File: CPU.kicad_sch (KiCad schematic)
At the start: 208 parts, among them P1 Conn_02x36_Top_Bottom, P10 Conn_02x08_Counter_Clockwise, P2 Conn_02x13_Top_Bottom, P3 Conn_02x13_Top_Bottom, P4 Conn_02x08_Counter_Clockwise, P5 Conn_02x25_Counter_Clockwise, P6 Conn_02x25_Counter_Clockwise, P7 Conn_02x07_Counter_Clockwise, P8 Conn_02x08_Counter_Clockwise

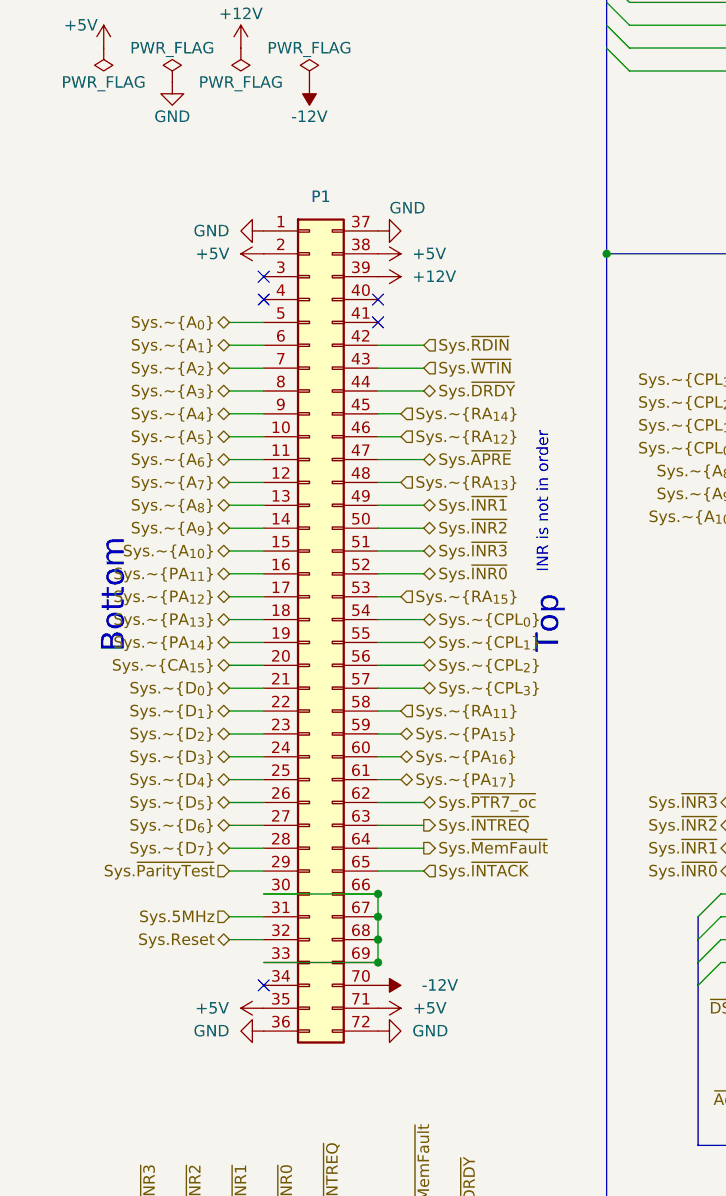
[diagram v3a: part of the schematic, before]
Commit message: Replace edge connector with pin headers
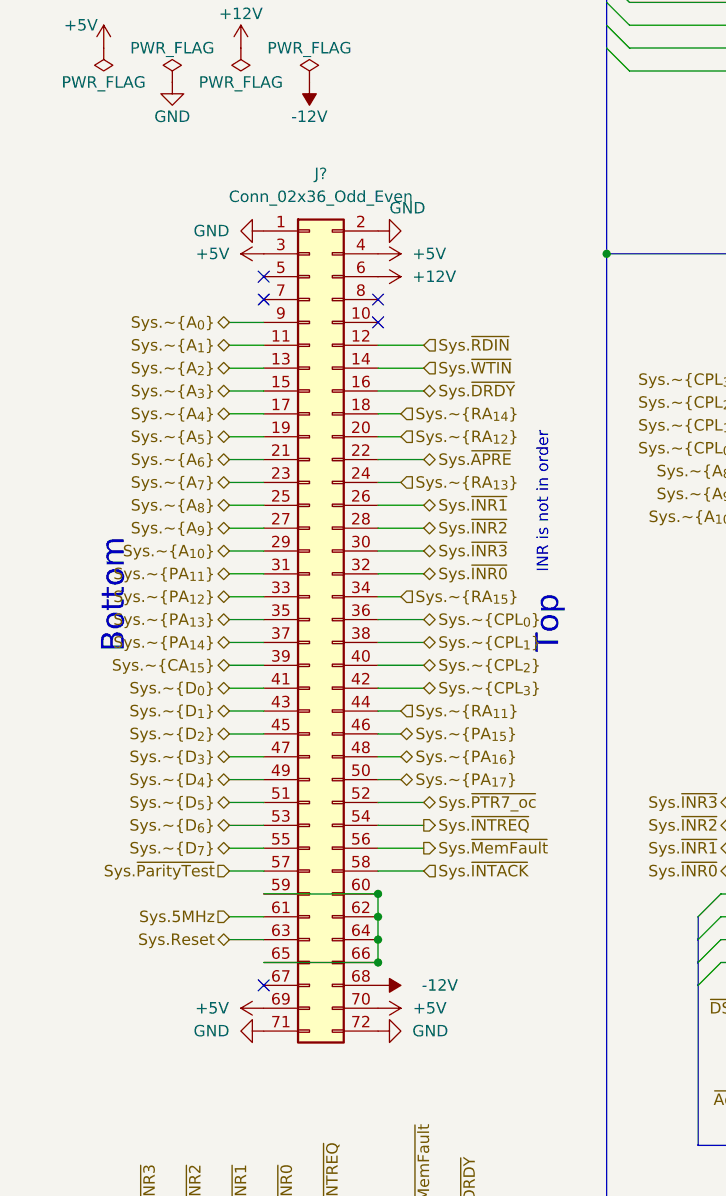
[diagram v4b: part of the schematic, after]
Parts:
- removed P1: Conn_02x36_Top_Bottom, Connector_PCBEdge:BUS_EE200, symbol Connector_Generic:Conn_02x36_Top_Bottom
- added J?: Conn_02x36_Odd_Even, Connector_PinHeader_2.54mm:PinHeader_2x36_P2.54mm_Horizontal, symbol Connector_Generic:Conn_02x36_Odd_Even
- U_D9: footprint (none) -> Package_DIP:DIP-16_W7.62mm
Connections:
- net +12V: now also J?.6 (Pin_6)
- net +5V: now also J?.3 (Pin_3), J?.4 (Pin_4), J?.69 (Pin_69), J?.70 (Pin_70)
- net -12V: now also J?.68 (Pin_68)
- net GND: now also J?.1 (Pin_1), J?.2 (Pin_2), J?.71 (Pin_71), J?.72 (Pin_72)
- net Sys.5MHz: now also J?.61 (Pin_61)
- net Sys.Reset: now also J?.63 (Pin_63)
- net Sys.~{APRE}: now also J?.22 (Pin_22)
- net Sys.~{A_{0}}: now also J?.9 (Pin_9)
- net Sys.~{A_{10}}: now also J?.29 (Pin_29)
- net Sys.~{A_{1}}: now also J?.11 (Pin_11)
- net Sys.~{A_{2}}: now also J?.13 (Pin_13)
- net Sys.~{A_{3}}: now also J?.15 (Pin_15)
- net Sys.~{A_{4}}: now also J?.17 (Pin_17)
- net Sys.~{A_{5}}: now also J?.19 (Pin_19)
- net Sys.~{A_{6}}: now also J?.21 (Pin_21)
- net Sys.~{A_{7}}: now also J?.23 (Pin_23)
- net Sys.~{A_{8}}: now also J?.25 (Pin_25)
- net Sys.~{A_{9}}: now also J?.27 (Pin_27)
- net Sys.~{CA_{15}}: now also J?.39 (Pin_39)
- net Sys.~{CPL_{0}}: now also J?.36 (Pin_36)
- net Sys.~{CPL_{1}}: now also J?.38 (Pin_38)
- net Sys.~{CPL_{2}}: now also J?.40 (Pin_40)
- net Sys.~{CPL_{3}}: now also J?.42 (Pin_42)
- net Sys.~{DRDY}: now also J?.16 (Pin_16)
- net Sys.~{D_{0}}: now also J?.41 (Pin_41)
- net Sys.~{D_{1}}: now also J?.43 (Pin_43)
- net Sys.~{D_{2}}: now also J?.45 (Pin_45)
- net Sys.~{D_{3}}: now also J?.47 (Pin_47)
- net Sys.~{D_{4}}: now also J?.49 (Pin_49)
- net Sys.~{D_{5}}: now also J?.51 (Pin_51)
- net Sys.~{D_{6}}: now also J?.53 (Pin_53)
- net Sys.~{D_{7}}: now also J?.55 (Pin_55)
- net Sys.~{INR0}: now also J?.32 (Pin_32)
- net Sys.~{INR1}: now also J?.26 (Pin_26)
- net Sys.~{INR2}: now also J?.28 (Pin_28)
- net Sys.~{INR3}: now also J?.30 (Pin_30)
- net Sys.~{INTACK}: now also J?.58 (Pin_58)
- net Sys.~{INTREQ}: now also J?.54 (Pin_54)
- net Sys.~{MemFault}: now also J?.56 (Pin_56)
- net Sys.~{PA_{11}}: now also J?.31 (Pin_31)
- net Sys.~{PA_{12}}: now also J?.33 (Pin_33)
- net Sys.~{PA_{13}}: now also J?.35 (Pin_35)
- net Sys.~{PA_{14}}: now also J?.37 (Pin_37)
- net Sys.~{PA_{15}}: now also J?.46 (Pin_46)
- net Sys.~{PA_{16}}: now also J?.48 (Pin_48)
- net Sys.~{PA_{17}}: now also J?.50 (Pin_50)
- net Sys.~{PTR7_oc}: now also J?.52 (Pin_52)
- net Sys.~{ParityTest}: now also J?.57 (Pin_57)
- net Sys.~{RA_{11}}: now also J?.44 (Pin_44)
- net Sys.~{RA_{12}}: now also J?.20 (Pin_20)
- net Sys.~{RA_{13}}: now also J?.24 (Pin_24)
- net Sys.~{RA_{14}}: now also J?.18 (Pin_18)
- net Sys.~{RA_{15}}: now also J?.34 (Pin_34)
- net Sys.~{RDIN}: now also J?.12 (Pin_12)
- net Sys.~{WTIN}: now also J?.14 (Pin_14)
- new net: J?.59 (Pin_59), J?.60 (Pin_60), J?.62 (Pin_62), J?.64 (Pin_64), J?.65 (Pin_65), J?.66 (Pin_66)
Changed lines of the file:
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@@
   (junction (at 548.64 353.06) (diameter 0) (color 0 0 0 0)
   )
-  (junction (at 58.42 454.66) (diameter 0) (color 0 0 0 0)
-  )
   (junction (at 243.84 285.75) (diameter 0) (color 0 0 0 0)
   )
@@
   (junction (at 1065.53 707.39) (diameter 0) (color 0 0 0 0)
   )
+  (junction (at 58.42 449.58) (diameter 0) (color 0 0 0 0)
+  )
   (junction (at 661.67 29.21) (diameter 0) (color 0 0 0 0)
   )
@@
   (junction (at 146.05 330.2) (diameter 0) (color 0 0 0 0)
   )
+  (junction (at 58.42 452.12) (diameter 0) (color 0 0 0 0)
+  )
   (junction (at 494.03 308.61) (diameter 0) (color 0 0 0 0)
   )
@@
   (junction (at 763.27 814.07) (diameter 0) (color 0 0 0 0)
   )
+  (junction (at 58.42 457.2) (diameter 0) (color 0 0 0 0)
+  )
   (junction (at 1158.24 657.86) (diameter 0) (color 0 0 0 0)
   )
@@
   (junction (at 1009.65 646.43) (diameter 0) (color 0 0 0 0)
   )
-  (junction (at 58.42 452.12) (diameter 0) (color 0 0 0 0)
-  )
   (junction (at 947.42 29.21) (diameter 0) (color 0 0 0 0)
   )
@@
   (junction (at 241.3 372.11) (diameter 0) (color 0 0 0 0)
   )
-  (junction (at 58.42 449.58) (diameter 0) (color 0 0 0 0)
-  )
   (junction (at 259.08 88.9) (diameter 0) (color 0 0 0 0)
   )
@@
   (junction (at 778.51 814.07) (diameter 0) (color 0 0 0 0)
   )
+  (junction (at 58.42 454.66) (diameter 0) (color 0 0 0 0)
+  )
   (junction (at 661.67 760.73) (diameter 0) (color 0 0 0 0)
   )
@@
   (junction (at 537.21 316.23) (diameter 0) (color 0 0 0 0)
   )
-  (junction (at 58.42 457.2) (diameter 0) (color 0 0 0 0)
-  )
   (junction (at 608.33 762) (diameter 0) (color 0 0 0 0)
   )
@@
     (stroke (width 0) (type default) (color 0 0 0 0))
   )
-  (wire (pts (xy 58.42 452.12) (xy 58.42 454.66))
-    (stroke (width 0) (type default) (color 0 0 0 0))
-  )
   (wire (pts (xy 737.87 433.07) (xy 773.43 433.07))
     (stroke (width 0) (type default) (color 0 0 0 0))
@@
     (stroke (width 0) (type default) (color 0 0 0 0))
   )
+  (wire (pts (xy 58.42 454.66) (xy 58.42 457.2))
+    (stroke (width 0) (type default) (color 0 0 0 0))
+  )
   (wire (pts (xy 201.93 50.8) (xy 212.09 50.8))
     (stroke (width 0) (type default) (color 0 0 0 0))
@@
     (stroke (width 0) (type default) (color 189 121 184 1))
   )
+  (wire (pts (xy 58.42 452.12) (xy 58.42 454.66))
+    (stroke (width 0) (type default) (color 0 0 0 0))
+  )
   (wire (pts (xy 267.97 331.47) (xy 327.66 331.47))
     (stroke (width 0) (type default) (color 0 0 0 0))
@@
     (stroke (width 0) (type default) (color 0 0 0 0))
   )
-  (wire (pts (xy 58.42 454.66) (xy 58.42 457.2))
-    (stroke (width 0) (type default) (color 0 0 0 0))
-  )
   (wire (pts (xy 793.75 692.15) (xy 793.75 697.23))
     (stroke (width 0) (type default) (color 0 0 0 0))
@@
     (pin "1")
   )
+  (symbol (lib_id "Connector_Generic:Conn_02x36_Odd_Even") (at 50.8 419.1 0) (unit 1)
+    (in_bom yes) (on_board yes) (fields_autoplaced)
+    (property "Reference" "J?" (id 0) (at 52.07 369.57 0))
+    (property "Value" "Conn_02x36_Odd_Even" (id 1) (at 52.07 372.11 0))
+    (property "Footprint" "Connector_PinHeader_2.54mm:PinHeader_2x36_P2.54mm_Horizontal" (id 2) (at 50.8 419.1 0)
+      (effects (font (size 1.27 1.27)) hide)
+    )
+    (property "Datasheet" "~" (id 3) (at 50.8 419.1 0)
+      (effects (font (size 1.27 1.27)) hide)
+    )
+    (pin "1")
+    (pin "10")
+    (pin "11")
+    (pin "12")
+    (pin "13")
+    (pin "14")
+    (pin "15")
+    (pin "16")
+    (pin "17")
+    (pin "18")
+    (pin "19")
+    (pin "2")
+    (pin "20")
+    (pin "21")
+    (pin "22")
+    (pin "23")
+    (pin "24")
+    (pin "25")
+    (pin "26")
+    (pin "27")
+    (pin "28")
+    (pin "29")
+    (pin "3")
+    (pin "30")
+    (pin "31")
+    (pin "32")
+    (pin "33")
+    (pin "34")
+    (pin "35")
+    (pin "36")
+    (pin "37")
+    (pin "38")
+    (pin "39")
+    (pin "4")
+    (pin "40")
+    (pin "41")
+    (pin "42")
+    (pin "43")
+    (pin "44")
+    (pin "45")
+    (pin "46")
+    (pin "47")
+    (pin "48")
+    (pin "49")
+    (pin "5")
+    (pin "50")
+    (pin "51")
+    (pin "52")
+    (pin "53")
+    (pin "54")
+    (pin "55")
+    (pin "56")
+    (pin "57")
+    (pin "58")
+    (pin "59")
+    (pin "6")
+    (pin "60")
+    (pin "61")
+    (pin "62")
+    (pin "63")
+    (pin "64")
+    (pin "65")
+    (pin "66")
+    (pin "67")
+    (pin "68")
+    (pin "69")
+    (pin "7")
+    (pin "70")
+    (pin "71")
+    (pin "72")
+    (pin "8")
+    (pin "9")
+  )
   (symbol (lib_id "Device:C_Small") (at 1032.51 683.26 0) (unit 1)
     (in_bom yes) (on_board yes)
@@
       (effects (font (size 1.27 1.27)) (justify left))
     )
-    (property "Footprint" "" (id 2) (at 276.86 149.86 0)
+    (property "Footprint" "Package_DIP:DIP-16_W7.62mm" (id 2) (at 276.86 149.86 0)
       (effects (font (size 1.27 1.27)) hide)
     )
@@
     (pin "2")
   )
-  (symbol (lib_id "Connector_Generic:Conn_02x36_Top_Bottom") (at 50.8 419.1 0) (unit 1)
-    (in_bom yes) (on_board yes)
-    (property "Reference" "P1" (id 0) (at 52.07 372.11 0))
-    (property "Value" "Conn_02x36_Top_Bottom" (id 1) (at 52.07 372.11 0)
-      (effects (font (size 1.27 1.27)) hide)
-    )
-    (property "Footprint" "Connector_PCBEdge:BUS_EE200" (id 2) (at 50.8 419.1 0)
-      (effects (font (size 1.27 1.27)) hide)
-    )
-    (property "Datasheet" "~" (id 3) (at 50.8 419.1 0)
-      (effects (font (size 1.27 1.27)) hide)
-    )
-    (pin "1")
-    (pin "10")
-    (pin "11")
-    (pin "12")
-    (pin "13")
-    (pin "14")
-    (pin "15")
-    (pin "16")
-    (pin "17")
-    (pin "18")
-    (pin "19")
-    (pin "2")
-    (pin "20")
-    (pin "21")
-    (pin "22")
-    (pin "23")
-    (pin "24")
-    (pin "25")
-    (pin "26")
-    (pin "27")
-    (pin "28")
-    (pin "29")
-    (pin "3")
-    (pin "30")
-    (pin "31")
-    (pin "32")
-    (pin "33")
-    (pin "34")
-    (pin "35")
-    (pin "36")
-    (pin "37")
-    (pin "38")
-    (pin "39")
-    (pin "4")
-    (pin "40")
-    (pin "41")
-    (pin "42")
-    (pin "43")
-    (pin "44")
-    (pin "45")
-    (pin "46")
-    (pin "47")
-    (pin "48")
-    (pin "49")
-    (pin "5")
-    (pin "50")
-    (pin "51")
-    (pin "52")
-    (pin "53")
-    (pin "54")
-    (pin "55")
-    (pin "56")
-    (pin "57")
-    (pin "58")
-    (pin "59")
-    (pin "6")
-    (pin "60")
-    (pin "61")
-    (pin "62")
-    (pin "63")
-    (pin "64")
-    (pin "65")
-    (pin "66")
-    (pin "67")
-    (pin "68")
-    (pin "69")
-    (pin "7")
-    (pin "70")
-    (pin "71")
-    (pin "72")
-    (pin "8")
-    (pin "9")
-  )
   (symbol (lib_id "74xx:74LS377") (at 745.49 679.45 90) (unit 1)
     (in_bom yes) (on_board yes)
@@
       (reference "DSW1") (unit 1) (value "SW_DIP_x08") (footprint "Button_Switch_THT:SW_DIP_SPSTx08_Slide_9.78x22.5mm_W7.62mm_P2.54mm")
     )
+    (path "/204a5142-3c33-4dca-b85e-682e0b14a381"
+      (reference "J?") (unit 1) (value "Conn_02x36_Odd_Even") (footprint "Connector_PinHeader_2.54mm:PinHeader_2x36_P2.54mm_Horizontal")
+    )
     (path "/25a6a420-d138-460a-9a95-c8a71db3148b"
       (reference "JP1") (unit 1) (value "Jumper_3_Open") (footprint "Connector_PinHeader_2.54mm:PinHeader_1x03_P2.54mm_Vertical")
     )
-    (path "/92693377-8797-4061-9050-b23a5d7a6ae4"
-      (reference "P1") (unit 1) (value "Conn_02x36_Top_Bottom") (footprint "Connector_PCBEdge:BUS_EE200")
-    )
     (path "/8e35be79-d4fb-43a5-9468-0d8e16e5fa6a"

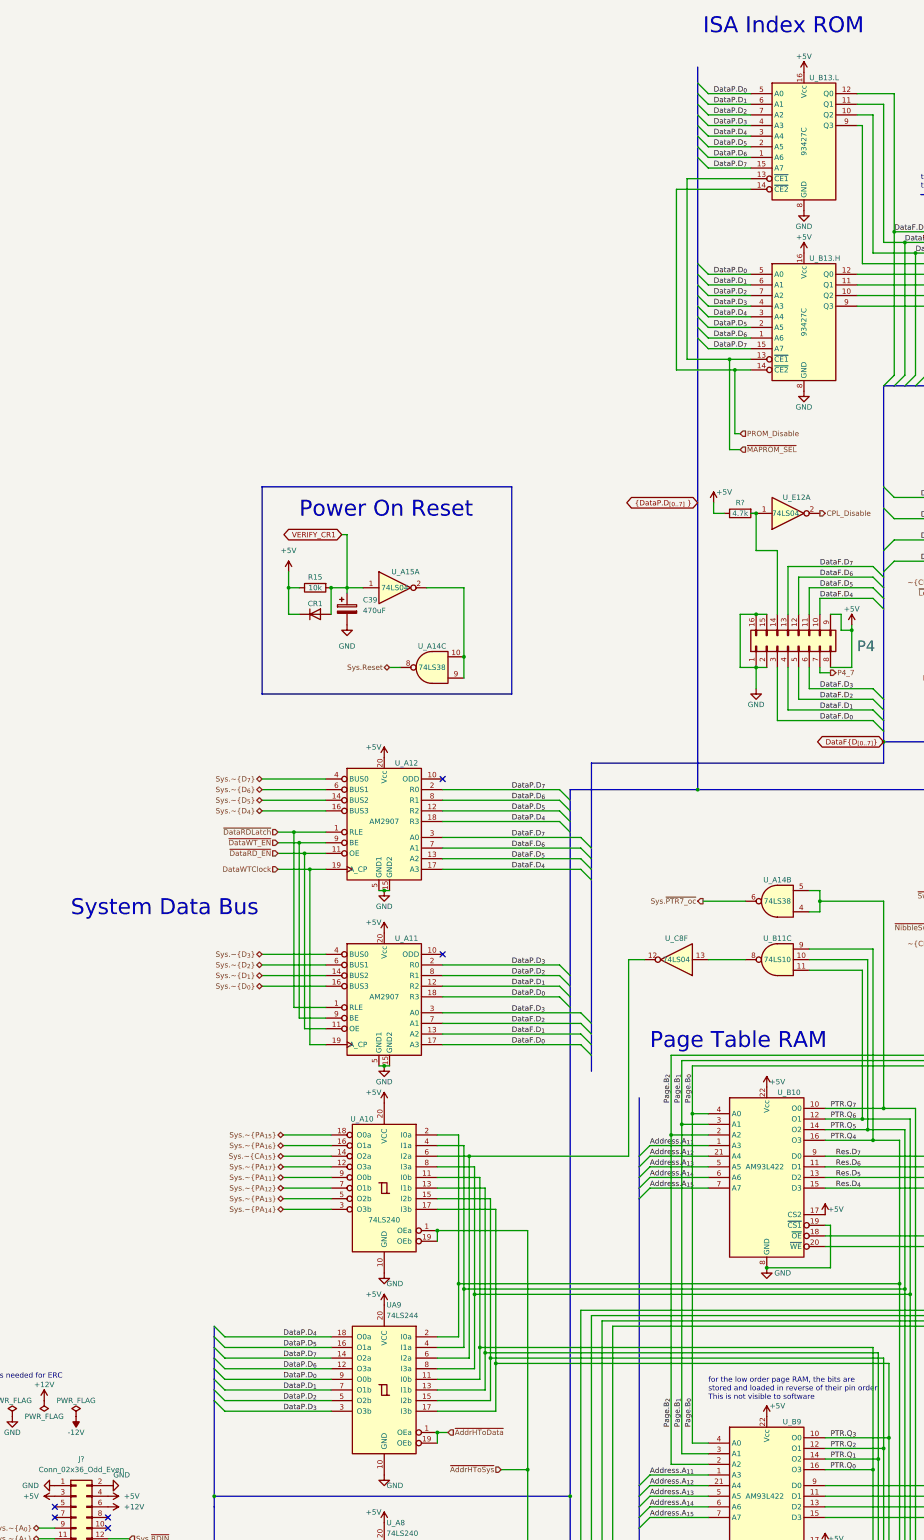
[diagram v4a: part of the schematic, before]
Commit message: Small fixes
Missing package definitions, some reference designator fixups
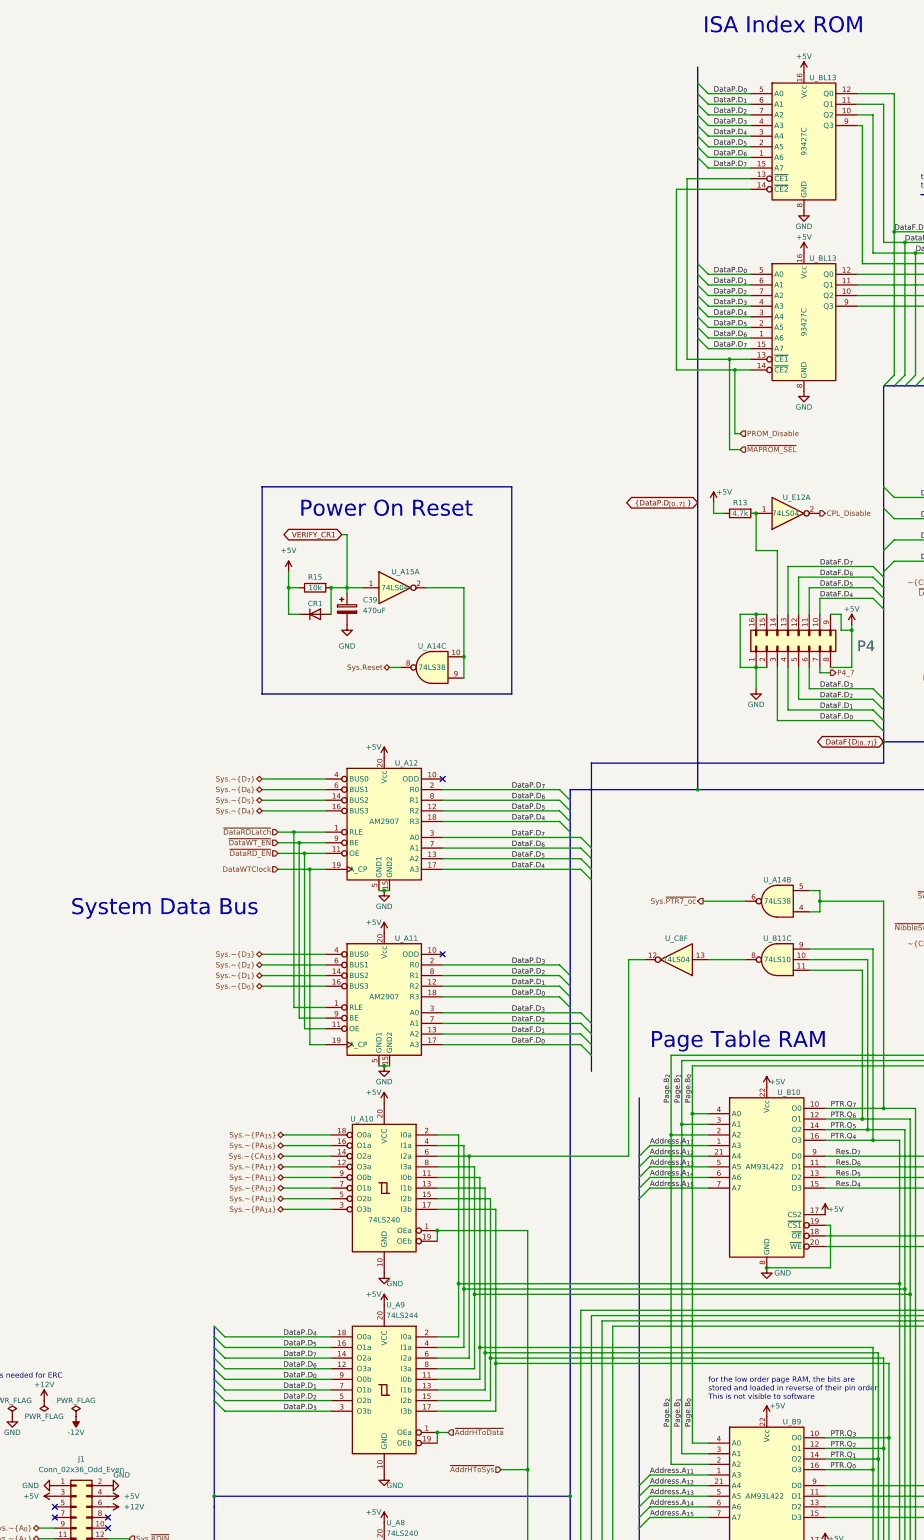
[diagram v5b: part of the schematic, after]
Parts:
- U_A4, U_A5, U_A6, U_A8: footprint (none) -> Package_DIP:DIP-20_W7.62mm
- U_A9: renamed from UA9; footprint (none) -> Package_DIP:DIP-20_W7.62mm
- gave numbers to parts that had none: 2
- renumbered U_B13.L to U_BL13, U_B13.H to U_BL13

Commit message: Fix ISA ROM designation
Replace russian 'C' letter with latin one. They look identical but have
different codes and UTF-8 characters in the .dsn file cause FreeRouting's
loader to crash
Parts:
- U_BL13: value 93427С -> 93427C
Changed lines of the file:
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@@
       (effects (font (size 1.27 1.27)) (justify left))
     )
-    (property "Value" "93427С" (id 1) (at 224.79 54.61 90))
+    (property "Value" "93427C" (id 1) (at 224.79 54.61 90))
     (property "Footprint" "Package_DIP:DIP-20_W7.62mm" (id 2) (at 247.65 29.21 0)
       (effects (font (size 1.27 1.27)) hide)
@@
       (effects (font (size 1.27 1.27)) (justify left))
     )
-    (property "Value" "93427С" (id 1) (at 224.79 97.79 90))
+    (property "Value" "93427C" (id 1) (at 224.79 97.79 90))
     (property "Footprint" "Package_DIP:DIP-20_W7.62mm" (id 2) (at 247.65 72.39 0)
       (effects (font (size 1.27 1.27)) hide)
@@
     )
     (path "/87f1dd62-191b-408d-8ad7-44a75dff6333"
-      (reference "U_BL13") (unit 1) (value "93427С") (footprint "Package_DIP:DIP-20_W7.62mm")
+      (reference "U_BL13") (unit 1) (value "93427C") (footprint "Package_DIP:DIP-20_W7.62mm")
     )
     (path "/c0266c95-ae17-45e2-bf80-9f2f693576d4"
-      (reference "U_BL13") (unit 1) (value "93427С") (footprint "Package_DIP:DIP-20_W7.62mm")
+      (reference "U_BL13") (unit 1) (value "93427C") (footprint "Package_DIP:DIP-20_W7.62mm")
     )
     (path "/8af415d4-268f-42b0-9c51-01a0acd645d3"
